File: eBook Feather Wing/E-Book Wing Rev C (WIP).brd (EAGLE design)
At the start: 77.5 x 112.3 mm, 96 parts, among them IC1 MCP23008/SO, IC2 23K256-I/SN, J1 MJ-3502N, Q1 IRLML0100, SW1 SPDT_SWITCH

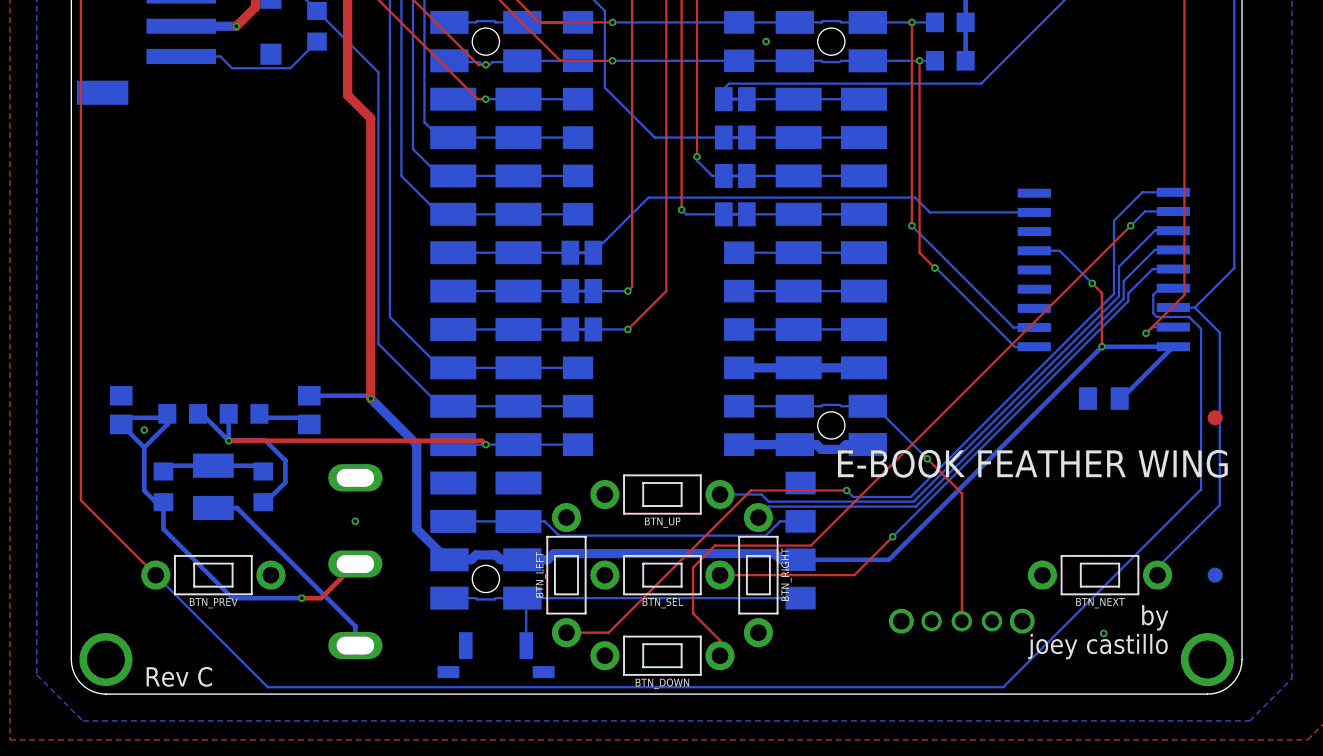
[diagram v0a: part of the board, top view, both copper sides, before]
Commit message: surface mount part swap, two more fiducials
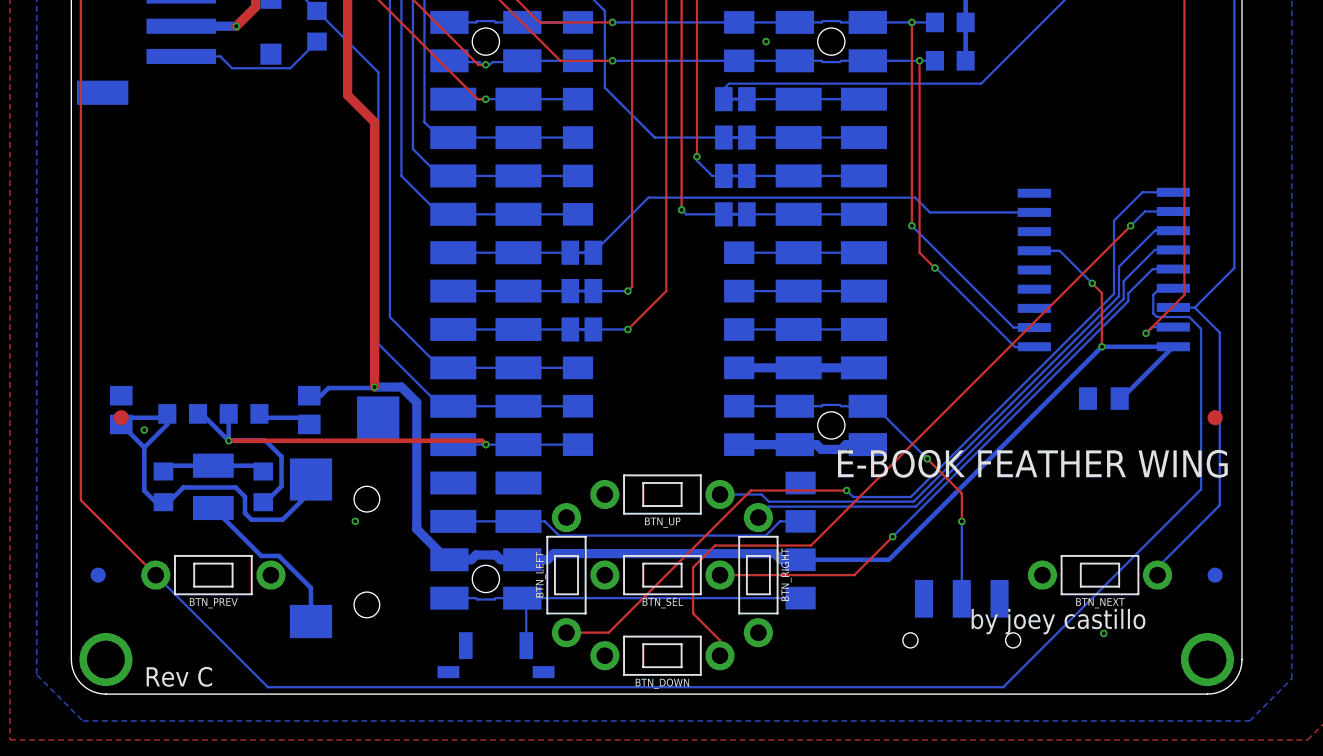
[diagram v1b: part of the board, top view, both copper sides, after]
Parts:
- removed SW1: SPDT_SWITCH, My Stuff:A10767
- added FID5, FID6: FIDUCIAL_1MM, microbuilder:FIDUCIAL_1MM
- added S1: JS102011SAQN, JS102011SAQN:SW_JS102011SAQN
- J1: value MJ-3502N -> MJ-3523-SMT; device MJ-3502N:CUI_MJ-3502N -> MJ-3523-SMT:CUI_MJ-3523-SMT
- moved J1 1.17 mm to (19.3, 9.65), turned to 270 degrees
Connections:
- net EN: now also S1.2; no longer SW1.P$2
- net GND: now also S1.1; no longer SW1.P$3
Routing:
- net AGND: track 30.1 -> 26.0 mm, vias 1 -> 0
- net AUDIO_OUT: track 13.9 -> 10.9 mm
- net EN: track 25.7 -> 24.2 mm, vias 1 -> 2
- net +3V3: track 367.4 -> 368.9 mm

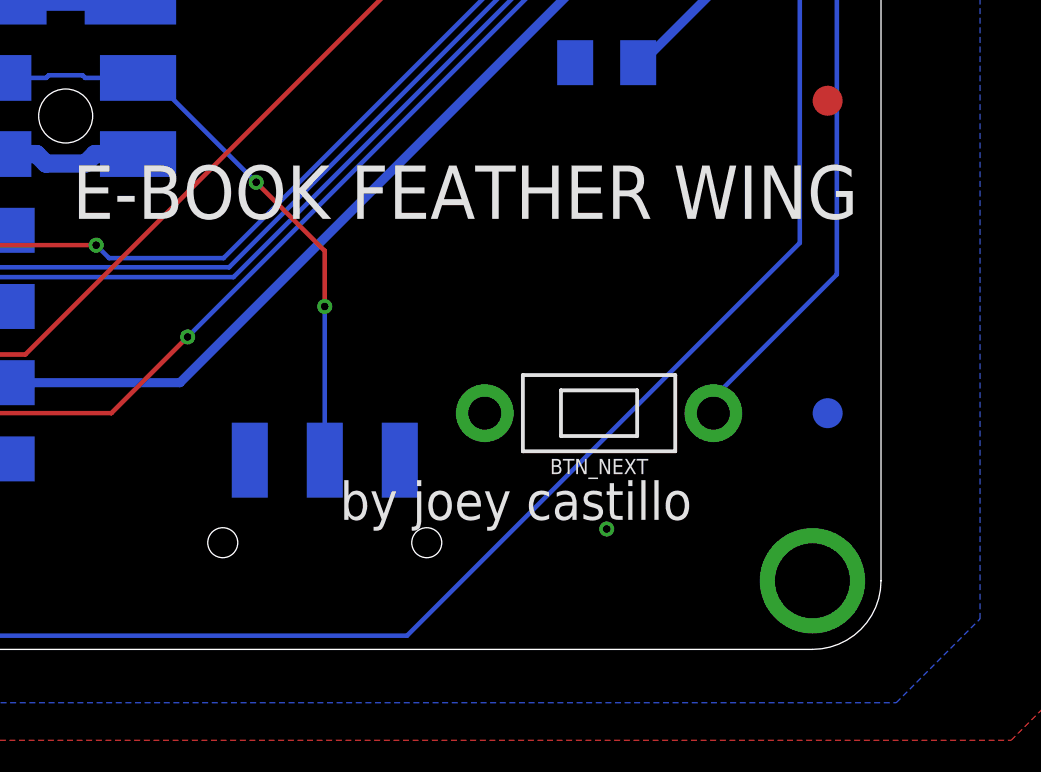
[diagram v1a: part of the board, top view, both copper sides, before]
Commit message: lol nevermind this thru-hole switch is cheaper
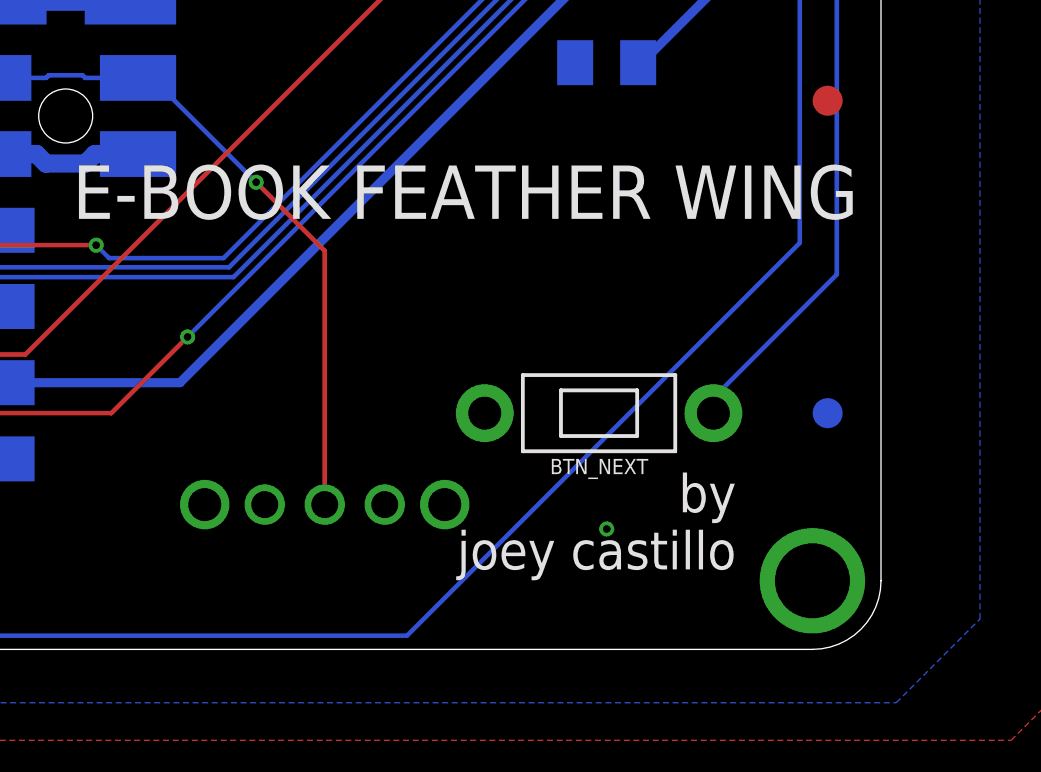
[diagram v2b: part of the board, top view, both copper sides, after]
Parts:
- removed S1: JS102011SAQN, JS102011SAQN:SW_JS102011SAQN
- added SW1: SPDT_SWITCH, My Stuff:A10767
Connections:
- net EN: now also SW1.P$2; no longer S1.2
- net GND: now also SW1.P$3; no longer S1.1
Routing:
- net EN: track 24.2 -> 25.7 mm, vias 2 -> 1
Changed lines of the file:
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@@
 <?xml version="1.0" encoding="utf-8"?>
 <!DOCTYPE eagle SYSTEM "eagle.dtd">
-<eagle version="9.3.0">
+<eagle version="9.4.2">
 <drawing>
 <settings>
@@
 <layer number="27" name="tValues" color="7" fill="1" visible="no" active="yes"/>
 <layer number="28" name="bValues" color="7" fill="1" visible="no" active="yes"/>
-<layer number="29" name="tStop" color="7" fill="3" visible="no" active="yes"/>
+<layer number="29" name="tStop" color="7" fill="3" visible="yes" active="yes"/>
 <layer number="30" name="bStop" color="7" fill="6" visible="no" active="yes"/>
 <layer number="31" name="tCream" color="7" fill="4" visible="no" active="yes"/>
@@
 19 Power Supply for
    OTP Programming (NC)</text>
-<text x="59.182" y="5.588" size="1.27" layer="21" font="vector" ratio="18" align="top-left">by joey castillo</text>
+<text x="72.39" y="5.842" size="1.27" layer="21" font="vector" ratio="18" align="top-right">by
+joey castillo</text>
 <text x="76.454" y="16.256" size="1.778" layer="22" font="vector" ratio="18" rot="MR0" align="top-left">E-BOOK
 FEATHER WING</text>
@@
 contacts on TOP.</text>
 <text x="68.072" y="1.27" size="0.8128" layer="22" font="vector" rot="MR0" align="top-center">CC-BY-SA 4.0</text>
-<text x="59.182" y="3.048" size="1.27" layer="29" font="vector" ratio="18" align="top-left">@josecastillo</text>
+<text x="72.39" y="2.032" size="1.27" layer="29" font="vector" ratio="18" align="top-right">@josecastillo</text>
 <wire x1="55.626" y1="-9.652" x2="34.29" y2="-9.652" width="0.0508" layer="22"/>
 <text x="22.098" y="36.068" size="0.8128" layer="22" font="vector" rot="MR0" align="top-left">The DAC on A0 drives mono
@@
 pass to the headphone jack,
 while blocking the DC component.</text>
-<text x="58.674" y="8.128" size="0.508" layer="22" font="vector" ratio="18" rot="MR0" align="center">ENABLE_SWITCH</text>
+<text x="58.674" y="3.302" size="0.508" layer="22" font="vector" ratio="18" rot="MR0" align="center">ENABLE_SWITCH</text>
 <text x="8.6614" y="110.744" size="0.508" layer="21" font="vector" ratio="18" rot="R180" align="center">GND</text>
 <text x="6.1214" y="110.744" size="0.508" layer="21" font="vector" ratio="18" rot="R180" align="center">RX</text>
@@
 <attribute name="VALUE" x="24.177040625" y="16.62635" size="1.270790625" layer="28" rot="MR270"/>
 </element>
-<element name="S1" library="JS102011SAQN" package="SW_JS102011SAQN" value="JS102011SAQN" x="58.674" y="3.556" smashed="yes" rot="MR0">
-<attribute name="DESCRIPTION" value=" JS10 Series SPDT On-On 6 V 0.3 A Gull Wing SMT Slide Switch " x="58.674" y="3.556" size="1.778" layer="28" rot="MR0" display="off"/>
-<attribute name="DIGI-KEY_PART_NUMBER" value="401-1999-1-ND" x="58.674" y="3.556" size="1.778" layer="28" rot="MR0" display="off"/>
-<attribute name="DIGI-KEY_PURCHASE_URL" value="https://www.digikey.com/product-detail/en/c-k/JS102011SAQN/401-1999-1-ND/1640114?utm_source=snapeda&amp;utm_medium=aggregator&amp;utm_campaign=symbol" x="58.674" y="3.556" size="1.778" layer="28" rot="MR0" display="off"/>
-<attribute name="MF" value="C&amp;K" x="58.674" y="3.556" size="1.778" layer="28" rot="MR0" display="off"/>
-<attribute name="MP" value="JS102011SAQN" x="58.674" y="3.556" size="1.778" layer="28" rot="MR0" display="off"/>
-<attribute name="NAME" x="63.47753125" y="0.5538" size="1.27093125" layer="26" rot="MR90"/>
-<attribute name="PACKAGE" value="None" x="58.674" y="3.556" size="1.778" layer="28" rot="MR0" display="off"/>
-<attribute name="VALUE" x="52.56866875" y="0.25311875" size="1.271109375" layer="28" rot="MR90"/>
-</element>
 <element name="FID5" library="microbuilder" package="FIDUCIAL_1MM" value="FIDUCIAL_1MM" x="1.524" y="7.874" smashed="yes" rot="MR0">
 <attribute name="BOM" value="EXCLUDE" x="1.524" y="7.874" size="1.778" layer="28" rot="MR0" display="off"/>
@@
 <element name="FID6" library="microbuilder" package="FIDUCIAL_1MM" value="FIDUCIAL_1MM" x="3.048" y="18.288" smashed="yes">
 <attribute name="BOM" value="EXCLUDE" x="3.048" y="18.288" size="1.778" layer="27" display="off"/>
+</element>
+<element name="SW1" library="My Stuff" package="A10767" value="SPDT_SWITCH" x="58.674" y="4.826" smashed="yes" rot="MR0">
+<attribute name="NAME" x="58.674" y="7.747" size="0.8128" layer="52" font="vector" ratio="18" rot="MR0" align="center"/>
 </element>
 </elements>
@@
 <via x="18.542" y="11.43" extent="1-16" drill="0.254"/>
 <via x="61.722" y="106.68" extent="1-16" drill="0.254"/>
-<contactref element="S1" pad="1"/>
+<contactref element="SW1" pad="P$3"/>
 </signal>
 <signal name="SD_CS">
@@
 <wire x1="56.388" y1="15.5702" x2="52.9082" y2="19.05" width="0.1524" layer="16"/>
 <wire x1="52.9082" y1="19.05" x2="52.451" y2="19.05" width="0.1524" layer="16"/>
-<contactref element="S1" pad="2"/>
-<wire x1="58.674" y1="6.306" x2="58.674" y2="11.43" width="0.1524" layer="16"/>
-<via x="58.674" y="11.43" extent="1-16" drill="0.254"/>
-<wire x1="58.674" y1="11.43" x2="58.674" y2="13.2842" width="0.1524" layer="1"/>
-<wire x1="58.674" y1="13.2842" x2="56.388" y2="15.5702" width="0.1524" layer="1"/>
+<wire x1="56.388" y1="15.5702" x2="58.674" y2="13.2842" width="0.1524" layer="1"/>
+<contactref element="SW1" pad="P$2"/>
+<wire x1="58.674" y1="13.2842" x2="58.674" y2="4.826" width="0.1524" layer="1"/>
 </signal>
 <signal name="AREF">
